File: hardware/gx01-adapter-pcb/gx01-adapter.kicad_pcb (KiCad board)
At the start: 2 copper layers, 65 x 56.5 mm, 11 parts, among them J1 Pi GPIO 40-pin, J2 LCD 20-pin IDC, J3 Fan 1, J4 Fan 2

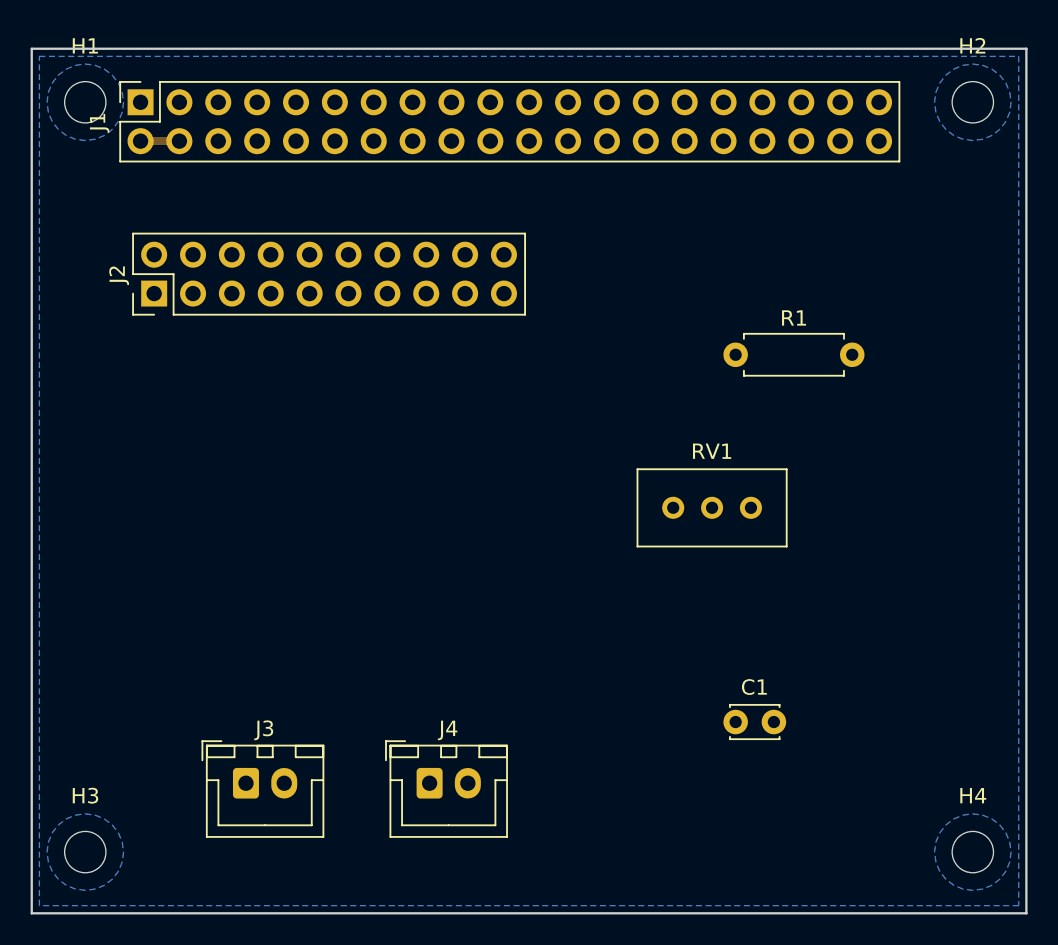
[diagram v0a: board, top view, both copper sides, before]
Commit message: refactor(pcb): switch LCD connector to 1x20 matching GDM12864H native layout
Significant layout iteration on the GX-01 adapter HAT:

- J2 changed from 2x10 IDC to 1x20 pin header — matches the GDM12864H's
  actual 1x20 solder pad layout (no ribbon-cable-to-LCD mapping needed)
- J1 and J2 now share pitch (2.54mm) and X origin (7.11mm), so pin pair k
  on J1 and pin k on J2 sit in the same vertical column. This makes
  GUI-based signal routing trivial: each LCD signal is a 1-2 segment
  short trace
- Re-mapped Pi GPIOs to LCD signals to use column-aligned pin pairs,
  avoiding LC29H-reserved pins (UART, I2C, PPS) and HAT ID EEPROM
- Moved passive components (RV1, R1, C1) to positions that enable direct
  analog trace routing
- Added VEE and BLA traces (now routed programmatically), plus 5V link
  between J1 pins 2/4 and straight down to J2 VDD
- V0 route left as ratsnest — its natural B.Cu path conflicts with C1's
  GND hole; GUI handles this in 30 seconds

Final DRC: 4 residual issues (all cosmetic — 1 courtyard overlap, 3 silk
clearance) + 15 unconnected items (ratsnest for GUI completion of 14
LCD signals + V0).

Re-rendered previews and re-exported complete Gerber set.

Co-Authored-By: Claude Opus 4.7 (1M context) <noreply@anthropic.com>
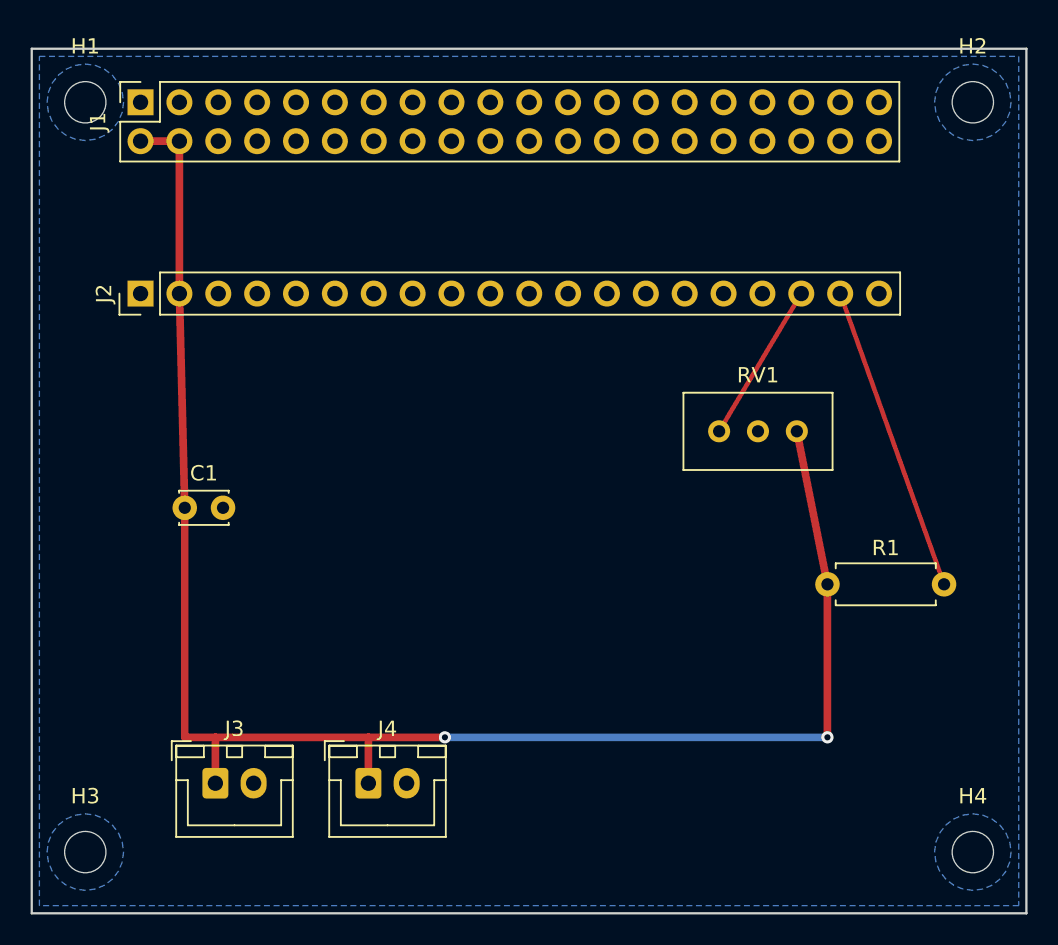
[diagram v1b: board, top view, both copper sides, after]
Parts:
- J2: value LCD 20-pin IDC -> LCD 20-pin; footprint PinHeader_2x10_P2.54mm_Vertical -> PinHeader_1x20_P2.54mm_Vertical
- moved C1 38.6 mm to (10.0, 30.0)
- moved R1 16.2 mm to (52.0, 35.0)
- moved RV1 5.83 mm to (50.0, 25.0)
- moved J4 4.00 mm to (22.0, 48.0)
- moved J3 2.00 mm to (12.0, 48.0)
- moved J2 0.89 mm to (7.11, 16.0)
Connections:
- J1 pad 16: LCD_CS1 -> (no net)
- J1 pad 18: LCD_CS2 -> LCD_DB0
- J1 pad 19: (no net) -> LCD_DB1
- J1 pad 22: LCD_RST -> LCD_DB2
- J1 pad 23: (no net) -> LCD_DB3
- J1 pad 26: (no net) -> LCD_DB4
- J1 pad 31: LCD_DB5 -> LCD_DB7
- J1 pad 32: LCD_DB4 -> (no net)
- J1 pad 33: LCD_DB3 -> LCD_CS1
- J1 pad 35: LCD_DB2 -> LCD_CS2
- J1 pad 36: LCD_DB1 -> (no net)
- J1 pad 37: LCD_DB0 -> LCD_RST
- J1 pad 40: LCD_DB7 -> LCD_DB5
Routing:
- net +5V: track 2.54 -> 109.7 mm, vias 0 -> 2
- net BLA: track 0.00 -> 20.2 mm
- net VEE: track 0.00 -> 10.5 mm

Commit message: feat(pcb): fully automated routing via FreeRouting integration
Adds autoroute.py to close the gap on programmatic signal routing.
Pipeline is now genuinely end-to-end: circuit.py → layout.py →
autoroute.py → DRC → Gerbers, with zero GUI interaction required.

Architecture:
- autoroute.py exports Specctra DSN from the unrouted .kicad_pcb
  via pcbnew.ExportSpecctraDSN
- Invokes FreeRouting 2.1.0 headlessly (java -Djava.awt.headless=true
  -jar freerouting-2.1.0.jar -de in.dsn -do out.ses -mp 50)
- Imports the resulting SES back into the board via
  pcbnew.ImportSpecctraSES
- Refills the GND zone (ZONE_FILLER.Fill) so the pour respects the
  newly-placed traces (critical — otherwise zone clearance violations)

Results for this design (15 unrouted nets, 20 total nets):
- 14 LCD signal traces routed as 45° paths between J1 and J2
- V0 trace routes RV1 wiper across to J2 pin 3 with 2 vias
- 5V distribution to all fan + passive pads completed
- 58 tracks total (up from 16 seed tracks)
- 0 unconnected items, 0 clearance violations
- Only 4 cosmetic warnings remain (courtyard overlap, silk clearance)

Runtime: ~15 seconds for autoroute.py with 50 passes. End-to-end
(circuit → fab-ready Gerbers) runs in ~90 seconds on a Pi 5.

Also committed: layout.py tweak (zone clearance 0.35→0.25mm to
match board default, eliminating thermal-relief conflicts near
adjacent routed signals); README fully rewritten to document the
automated pipeline; tools/freerouting-2.1.0.jar vendored so the
pipeline works without internet on future runs.

This answers the "can we fully automate PCB routing?" question with
an empirical yes for 2-layer boards of this density. FreeRouting's
2.1.0 release handles ~200-net designs at similar quality; the limit
scales with board complexity rather than being a hard cutoff at
hobby-scale projects.

Co-Authored-By: Claude Opus 4.7 (1M context) <noreply@anthropic.com>
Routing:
- net V0: track 0.00 -> 39.0 mm
- net LCD_DB5: track 0.00 -> 24.4 mm
- net LCD_RW: track 0.00 -> 14.6 mm
- net LCD_E: track 0.00 -> 14.6 mm
- net LCD_RST: track 0.00 -> 14.6 mm
- net LCD_RS: track 0.00 -> 14.6 mm
- net LCD_DB7: track 0.00 -> 14.6 mm
- net LCD_DB6: track 0.00 -> 14.6 mm
- net LCD_DB3: track 0.00 -> 14.6 mm
- net LCD_DB1: track 0.00 -> 14.6 mm
- net LCD_CS2: track 0.00 -> 14.6 mm
- net LCD_CS1: track 0.00 -> 14.6 mm
- net LCD_DB4: track 0.00 -> 12.1 mm
- net LCD_DB2: track 0.00 -> 12.1 mm
- net LCD_DB0: track 0.00 -> 12.1 mm
